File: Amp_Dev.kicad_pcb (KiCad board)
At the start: 2 copper layers, 100 x 100 mm, 0 parts

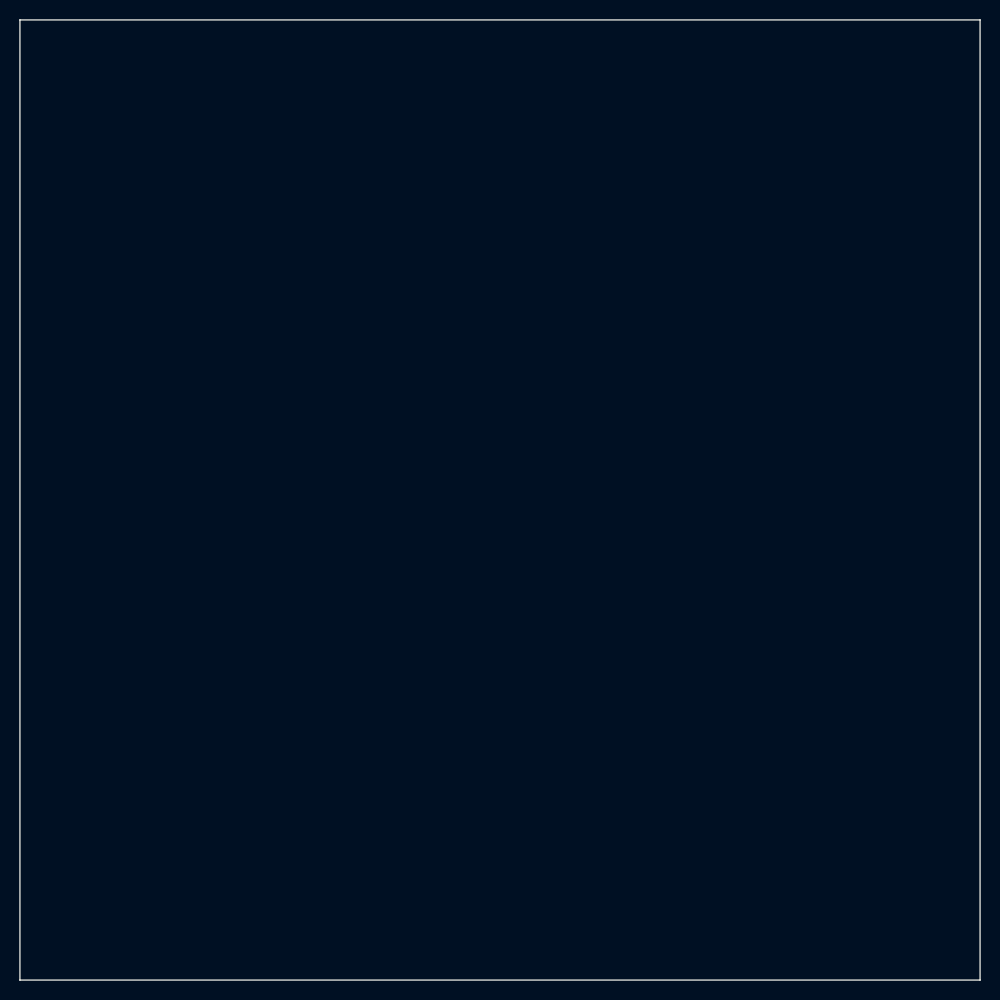
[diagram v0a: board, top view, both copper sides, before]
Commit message: Generated netlist for LNA components
Also added flood planes to top and bottom of board, and did initial LNA component placement
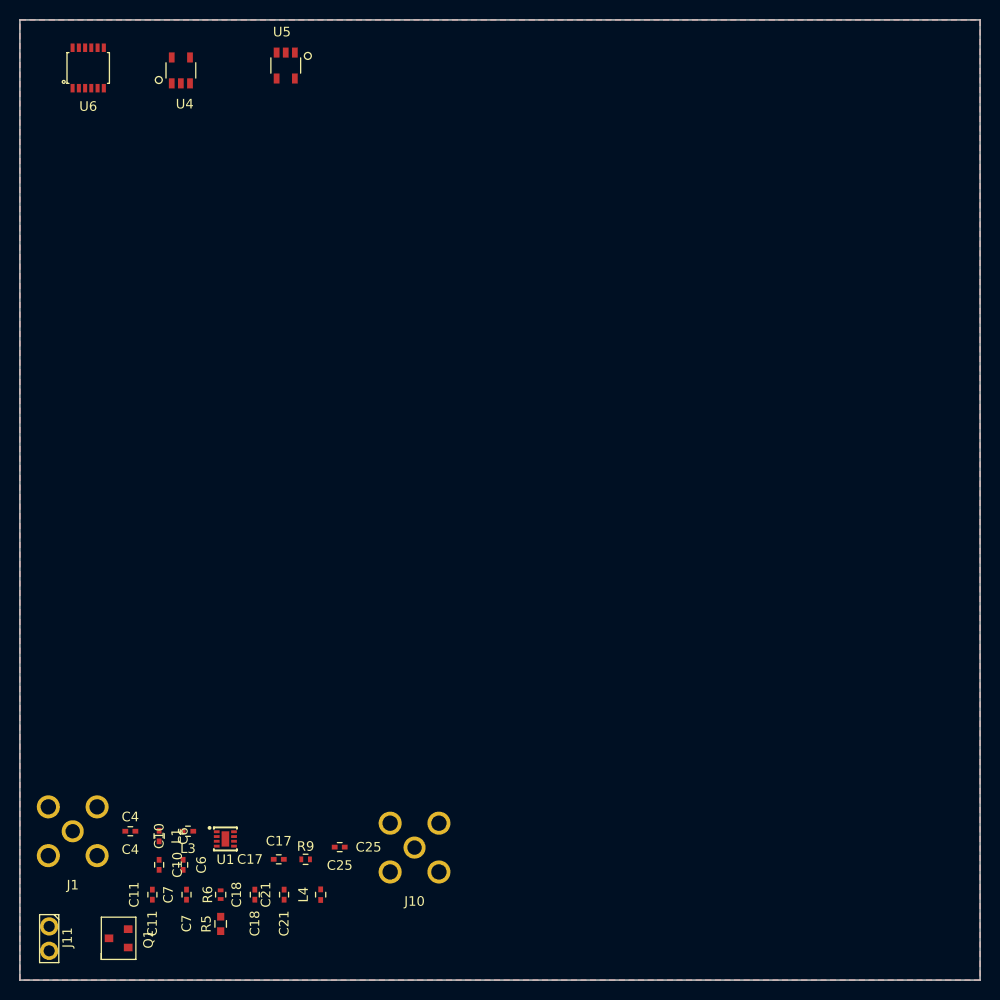
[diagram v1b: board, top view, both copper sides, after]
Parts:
- added C10: 0.01uF, SFUSat:C_0402, F.Cu at (114.5, 138.0)
- added C11: 56pF, SFUSat:C_0402, F.Cu at (113.8, 141.1)
- added C17: 56pF, SFUSat:C_0402, F.Cu at (127.0, 137.4)
- added C18: 390pF, SFUSat:C_0402, F.Cu at (124.5, 141.1)
- added C21: 0.1uF, SFUSat:C_0402, F.Cu at (127.5, 141.1)
- added C25: 100pF, SFUSat:C_0402, F.Cu at (133.3, 136.2)
- added C4: 100pF, SFUSat:C_0402, F.Cu at (111.5, 134.5)
- added C6: 390pF, SFUSat:C_0402, F.Cu at (117.0, 138.0)
- added C7: 0.01uF, SFUSat:C_0402, F.Cu at (117.4, 141.1)
- added J1: SMA, SFUSat:SMA-Vert-TH, F.Cu at (105.5, 134.5)
- added J10: SMA, SFUSat:SMA-Vert-TH, F.Cu at (141.1, 136.2)
- added J11: CONN_01X02, SFUSat:2x01In_Header_v2, F.Cu at (103.0, 145.7)
- added L1: 22nH, SFUSat:L_0402, F.Cu at (114.5, 135.0)
- added L3: 4.3nH, SFUSat:L_0402, F.Cu at (117.5, 134.5)
- added L4: 24nH, SFUSat:L_0402, F.Cu at (131.3, 141.1)
- added Q1: DMN2075U, SFUSat:SOT23_DMN2075U, F.Cu at (110.3, 145.6)
- added R5: 0R05, SFUSat:C_0603, F.Cu at (120.9, 144.2)
- added R6: 1210, SFUSat:R_0402, F.Cu at (120.9, 141.1)
- added R9: 100, SFUSat:R_0402, F.Cu at (129.8, 137.4)
- added U1: MML09211H, SFUSat:8-VFDFN, F.Cu at (121.4, 135.3)
- added U4: SN74LVC1G17, SFUSat:SOT_23_5, F.Cu at (116.8, 55.3)
- added U5: TLV702, SFUSat:SOT_23_5, F.Cu at (127.7, 54.8)
- added U6: LTC2644, SFUSat:12-TSSOP, F.Cu at (107.1, 55.0)
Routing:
- added copper zone on B.Cu, net GND
- added copper zone on F.Cu, net GND

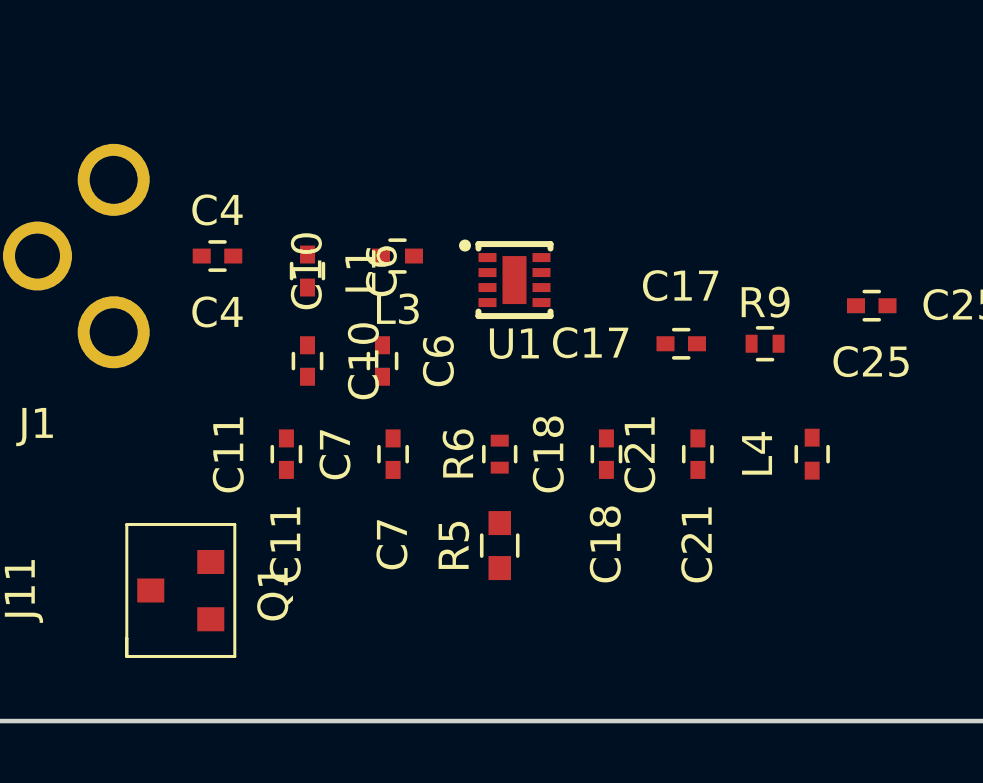
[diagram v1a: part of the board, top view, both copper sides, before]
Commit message: Refreshed footprints to add refdes to inductors and resistors
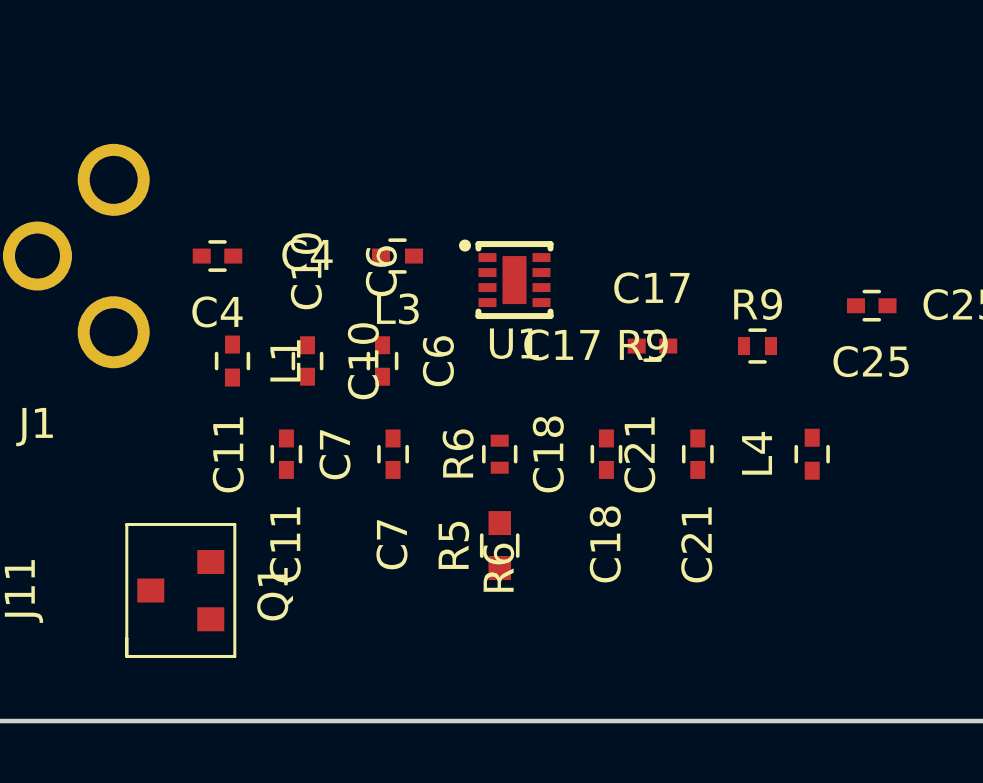
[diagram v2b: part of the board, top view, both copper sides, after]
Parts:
- moved L1 3.91 mm to (112.0, 138.0)
- moved C17 0.96 mm to (126.0, 137.5)
- moved R9 0.26 mm to (129.5, 137.5)
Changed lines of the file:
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@@
       (effects (font (size 1 1) (thickness 0.15)))
     )
-    (fp_text user %R (at 0 1.5 180) (layer F.SilkS)
+    (fp_text user %R (at -3 0 180) (layer F.SilkS)
       (effects (font (size 1 1) (thickness 0.15)))
     )
@@
   )
   (module SFUSat:C_0402 (layer F.Cu)
-    (at 126.958 137.424)
+    (at 126 137.5)
     (descr "Capacitor SMD 0402, reflow soldering, AVX (see smccp.pdf)")
     (tags "capacitor 0402")
@@
   )
   (module SFUSat:L_0402 (layer F.Cu)
-    (at 114.5 135 270)
+    (at 112 138 270)
     (descr "Resistor SMD 0402, reflow soldering, Vishay (see dcrcw.pdf)")
     (tags "resistor 0402")
@@
     )
     (fp_text value 22nH (at 0 1.8 270) (layer F.Fab)
+      (effects (font (size 1 1) (thickness 0.15)))
+    )
+    (fp_text user %R (at 0 -1.8 270) (layer F.Fab)
+      (effects (font (size 1 1) (thickness 0.15)))
+    )
+    (fp_text user %R (at -2.032 0 270) (layer F.SilkS)
       (effects (font (size 1 1) (thickness 0.15)))
     )
@@
       (effects (font (size 1 1) (thickness 0.15)))
     )
+    (fp_text user %R (at 0 -1.8 180) (layer F.Fab)
+      (effects (font (size 1 1) (thickness 0.15)))
+    )
+    (fp_text user %R (at -2.032 0 180) (layer F.SilkS)
+      (effects (font (size 1 1) (thickness 0.15)))
+    )
     (fp_line (start -0.5 0.25) (end -0.5 -0.25) (layer F.Fab) (width 0.1))
     (fp_line (start 0.5 0.25) (end -0.5 0.25) (layer F.Fab) (width 0.1))
@@
     )
     (fp_text value 24nH (at 0 1.8 90) (layer F.Fab)
+      (effects (font (size 1 1) (thickness 0.15)))
+    )
+    (fp_text user %R (at 0 -1.8 90) (layer F.Fab)
+      (effects (font (size 1 1) (thickness 0.15)))
+    )
+    (fp_text user %R (at -2.032 0 90) (layer F.SilkS)
       (effects (font (size 1 1) (thickness 0.15)))
     )
@@
       (effects (font (size 1 1) (thickness 0.15)))
     )
+    (fp_text user %R (at -3.81 0 90) (layer F.SilkS)
+      (effects (font (size 1 1) (thickness 0.15)))
+    )
     (fp_text user %R (at 0 -1.35 90) (layer F.Fab)
       (effects (font (size 1 1) (thickness 0.15)))
@@
   )
   (module SFUSat:R_0402 (layer F.Cu)
-    (at 129.752 137.424)
+    (at 129.5 137.5)
     (descr "Resistor SMD 0402, reflow soldering, Vishay (see dcrcw.pdf)")
     (tags "resistor 0402")
@@
       (effects (font (size 1 1) (thickness 0.15)))
     )
+    (fp_text user %R (at -3.81 0) (layer F.SilkS)
+      (effects (font (size 1 1) (thickness 0.15)))
+    )

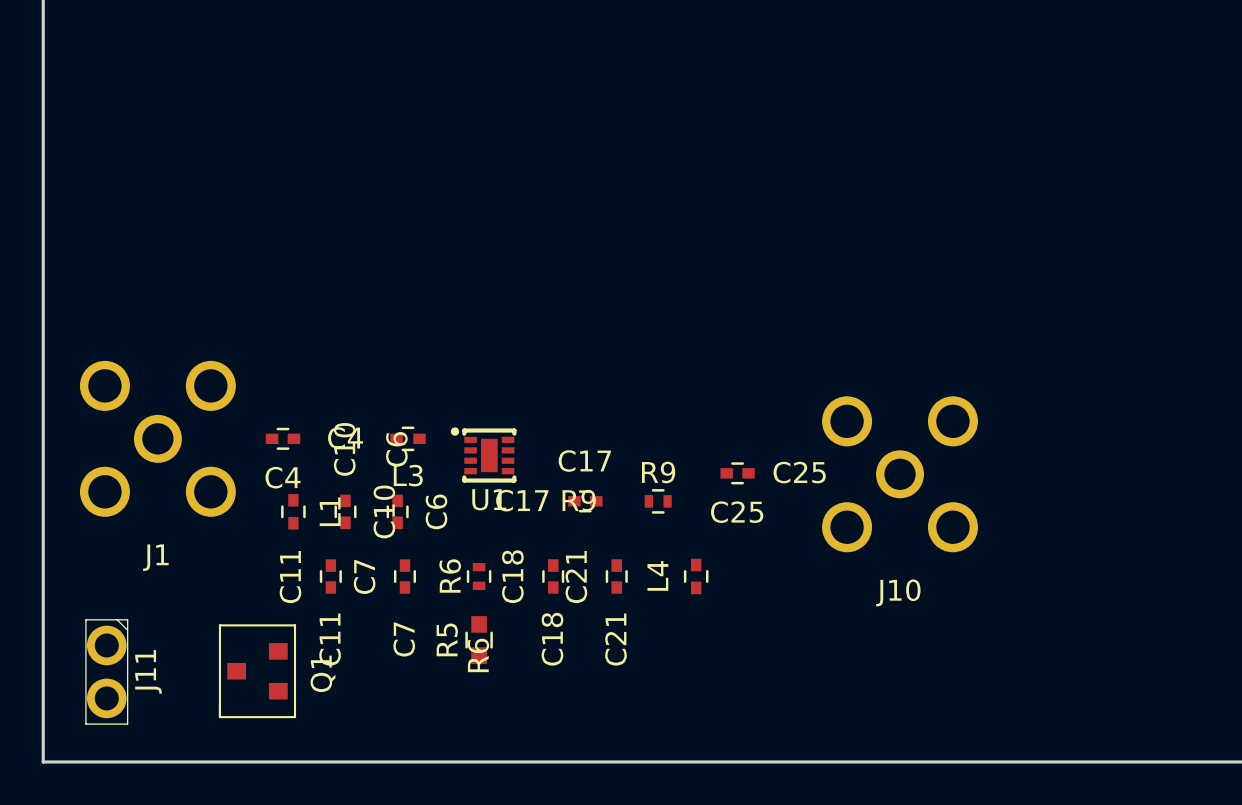
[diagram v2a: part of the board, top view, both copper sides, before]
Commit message: Updated layout
-Changed board thickness to 0.6 mm
-Used 0.7 mm RF trace width, resulting in 51.8 ohm impedance
-Used 0.5 mm power trace width, which is good for about 1.5 A
-Routed all LNA-related components
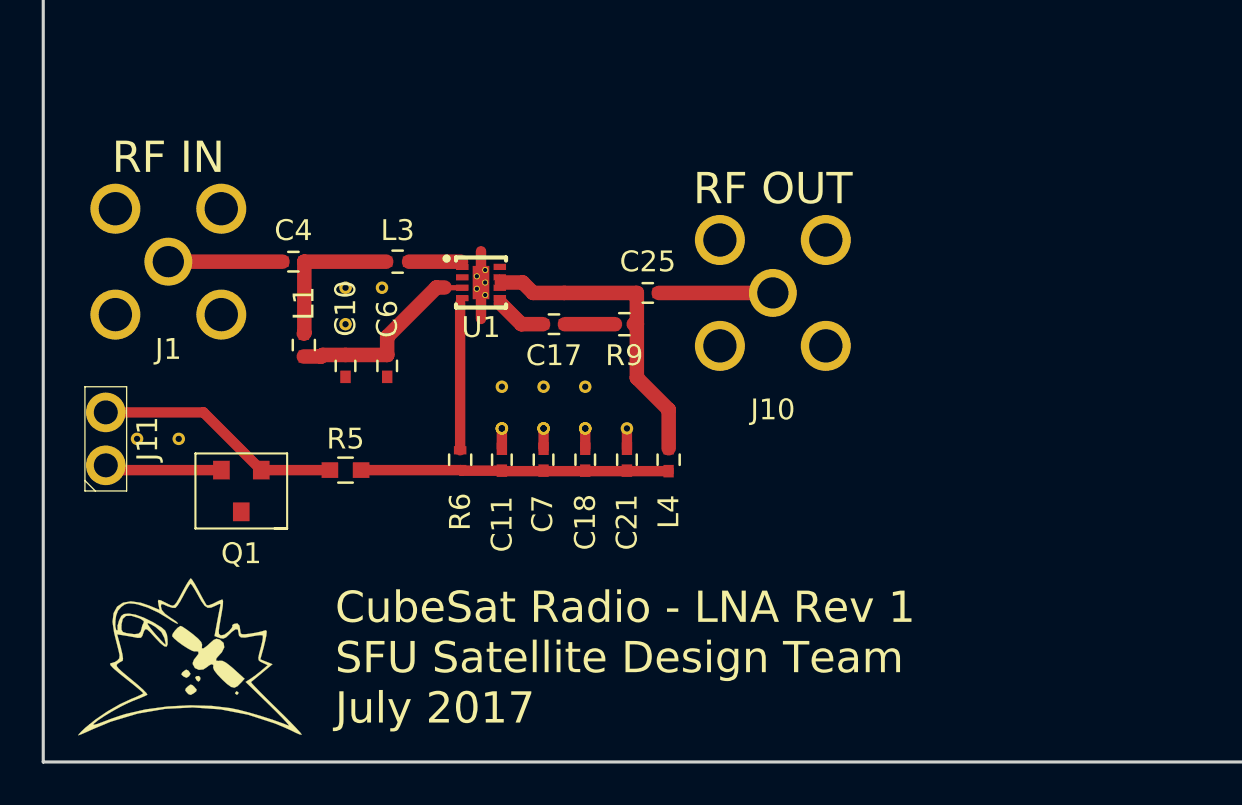
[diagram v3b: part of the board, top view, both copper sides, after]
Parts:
- added G***: LOGO, SFUSat:SFUSat_15mm_2, F.Cu at (107.0, 145.0)
- added REF** (x2): VIA-0.6mm, SFUSat:VIA-0.6mm, F.Cu at (122.0, 134.0)
- added REF**: VIA-0.6mm, SFUSat:VIA-0.6mm, F.Cu at (122.0, 132.0)
- added REF**: VIA-0.6mm, SFUSat:VIA-0.6mm, F.Cu at (124.0, 132.0)
- added REF**: VIA-0.6mm, SFUSat:VIA-0.6mm, F.Cu at (126.0, 132.0)
- added REF** (x2): VIA-0.6mm, SFUSat:VIA-0.6mm, F.Cu at (124.0, 134.0)
- added REF** (x2): VIA-0.6mm, SFUSat:VIA-0.6mm, F.Cu at (126.0, 134.0)
- added REF**: VIA-0.6mm, SFUSat:VIA-0.6mm, F.Cu at (128.0, 134.0)
- added REF**: VIA-0.6mm, SFUSat:VIA-0.6mm, F.Cu at (114.5, 129.0)
- added REF**: VIA-0.6mm, SFUSat:VIA-0.6mm, F.Cu at (114.5, 127.2)
- added REF**: VIA-0.6mm, SFUSat:VIA-0.6mm, F.Cu at (116.2, 127.2)
- added REF**: VIA-0.6mm, SFUSat:VIA-0.6mm, F.Cu at (104.5, 134.5)
- added REF**: VIA-0.6mm, SFUSat:VIA-0.6mm, F.Cu at (106.5, 134.5)
- moved J11 11.2 mm to (103.0, 134.5), turned to 90 degrees
- moved J10 10.6 mm to (135.0, 127.5)
- moved R5 10.4 mm to (114.5, 136.0), turned to 0 degrees
- moved C11 9.94 mm to (122.0, 135.5)
- moved C25 9.67 mm to (129.0, 127.5)
- moved C7 8.69 mm to (124.0, 135.5)
- moved Q1 8.68 mm to (109.5, 137.0), turned to 180 degrees
- moved R9 8.65 mm to (127.9, 129.0), turned to 180 degrees
- moved C17 8.63 mm to (124.5, 129.0), turned to 180 degrees
- moved C4 8.51 mm to (112.0, 126.0)
- moved J1 8.51 mm to (106.0, 126.0)
- moved L3 8.51 mm to (117.0, 126.0)
- moved U1 8.31 mm to (121.0, 127.0)
- moved L1 8.02 mm to (112.5, 130.0)
- moved C6 7.02 mm to (116.5, 131.0)
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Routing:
- net Net-(C25-Pad2): track 0.00 -> 15.4 mm
- net Net-(C11-Pad1): track 0.00 -> 14.8 mm
- net /LNA_5V0: track 0.00 -> 11.9 mm
- net Net-(C10-Pad1): track 0.00 -> 9.49 mm
- net Net-(C4-Pad1): track 0.00 -> 7.39 mm
- net Net-(R6-Pad2): track 0.00 -> 7.34 mm
- net GND: track 0.00 -> 7.15 mm
- net Net-(J11-Pad1): track 0.00 -> 5.65 mm
- net Net-(C4-Pad2): track 0.00 -> 5.47 mm
- net Net-(C25-Pad1): track 0.00 -> 5.47 mm
- net Net-(L3-Pad1): track 0.00 -> 2.76 mm
- net Net-(C17-Pad2): track 0.00 -> 2.72 mm
- net Net-(C17-Pad1): track 0.00 -> 2.40 mm
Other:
- net class Power added: clearance 0.2, trace_width 0.5, via_dia 0.6, via_drill 0.4
- net class RF added: clearance 0.2, trace_width 0.7, via_dia 0.6, via_drill 0.4
- board text added: "CubeSat Radio - LNA Rev 1 SFU Satellite Design Team July 2017"
- board text added: "RF IN"
- board text added: "RF OUT"
